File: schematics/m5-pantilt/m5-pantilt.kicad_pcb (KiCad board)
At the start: 2 copper layers, 50 x 50 mm, 28 parts, among them J1 Conn_02x15_Odd_Even, J2 Conn_02x03_Odd_Even, J3 Conn_02x03_Odd_Even, J4 Conn_01x04, J5 BAT, J6 Conn_01x04, J7 5V_POWER, SW1 SW_SPDT, U1 NL27WZ125

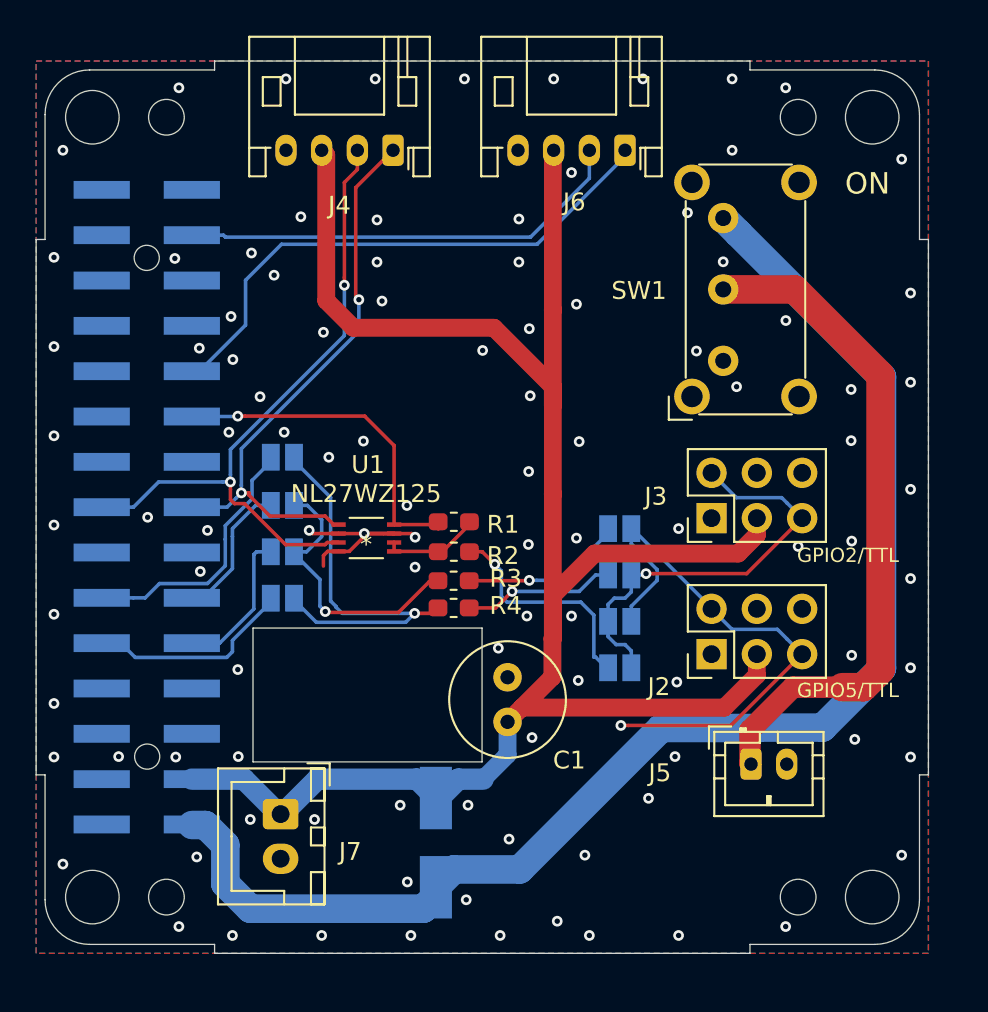
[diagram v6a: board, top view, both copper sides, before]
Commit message: Update to v0.2.0
Support another Three-State Bus Buffers, TC7WH241FK
Add description to schematic and PCB
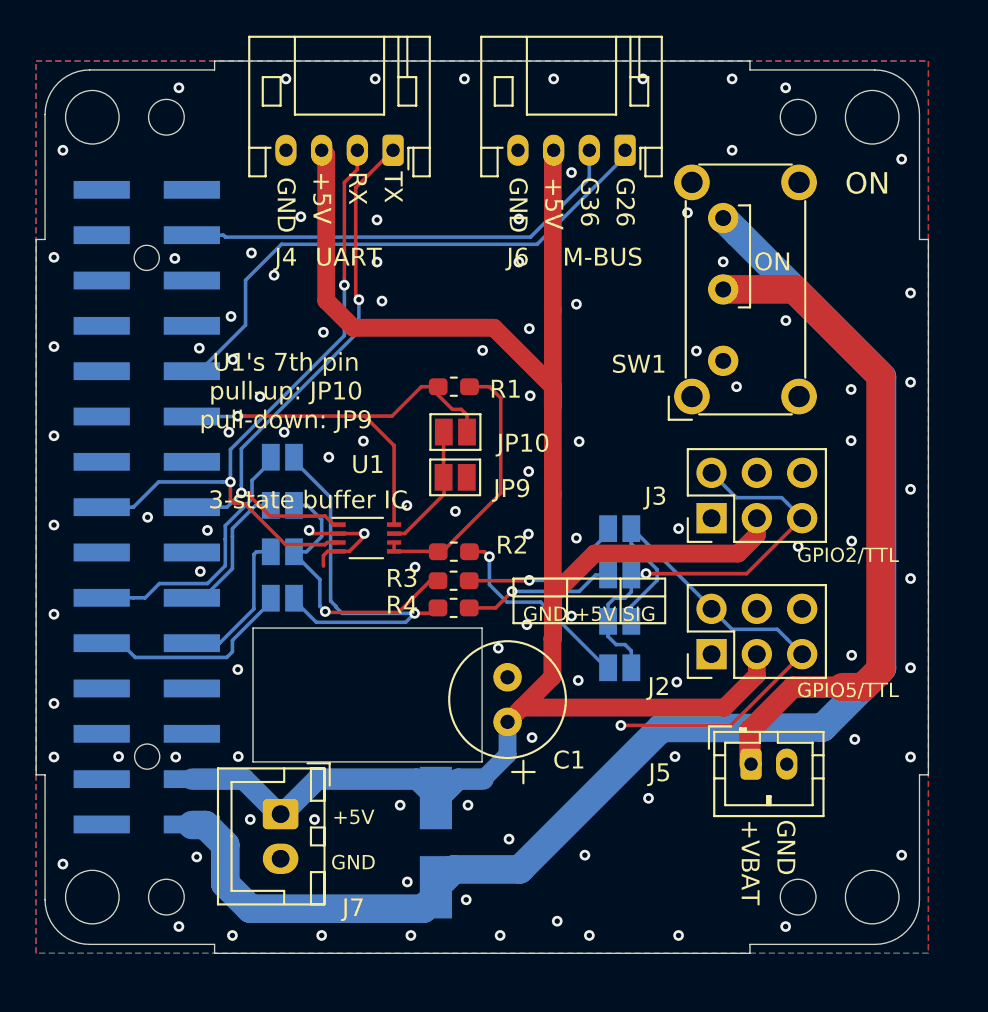
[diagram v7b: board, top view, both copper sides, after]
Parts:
- added JP10: Jumper_2_Open, Jumper:SolderJumper-2_P1.3mm_Open_Pad1.0x1.5mm, F.Cu at (123.5, 70.8)
- added JP9: Jumper_2_Open, Jumper:SolderJumper-2_P1.3mm_Open_Pad1.0x1.5mm, F.Cu at (123.5, 73.3)
- U1: value NL27WZ125 -> TC7WH241FK
- moved R1 7.57 mm to (123.4, 68.2)
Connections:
- U1 pad 7: GND -> Net-(JP10-Pad2)
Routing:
- net Net-(R1-Pad2): track 5.20 -> 15.4 mm
- net Net-(JP10-Pad2): track 0.00 -> 7.92 mm
- net +3V3: track 19.0 -> 25.1 mm
- net GND: track 11.2 -> 6.71 mm
- net Net-(JP4-Pad2): track 12.7 -> 11.4 mm
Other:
- board text added: "+5V"
- board text added: "+VBAT"
- board text added: "3-state buffer IC"
- board text added: "G26"
- board text added: "G36"
- board text added: "GND"
- board text added: "GND +5V SIG"
- board text added: "M-BUS"
- board text added: "RX"
- board text added: "TX"
- board text added: "U1's 7th pin pull-up: JP10 pull-down: JP9"
- board text added: "UART"
- board text added: "m5-pantilt board v0.2.0 @meganetaaan"
- board text removed: "m5-pantilt board v0.1.1 @meganetaaan"

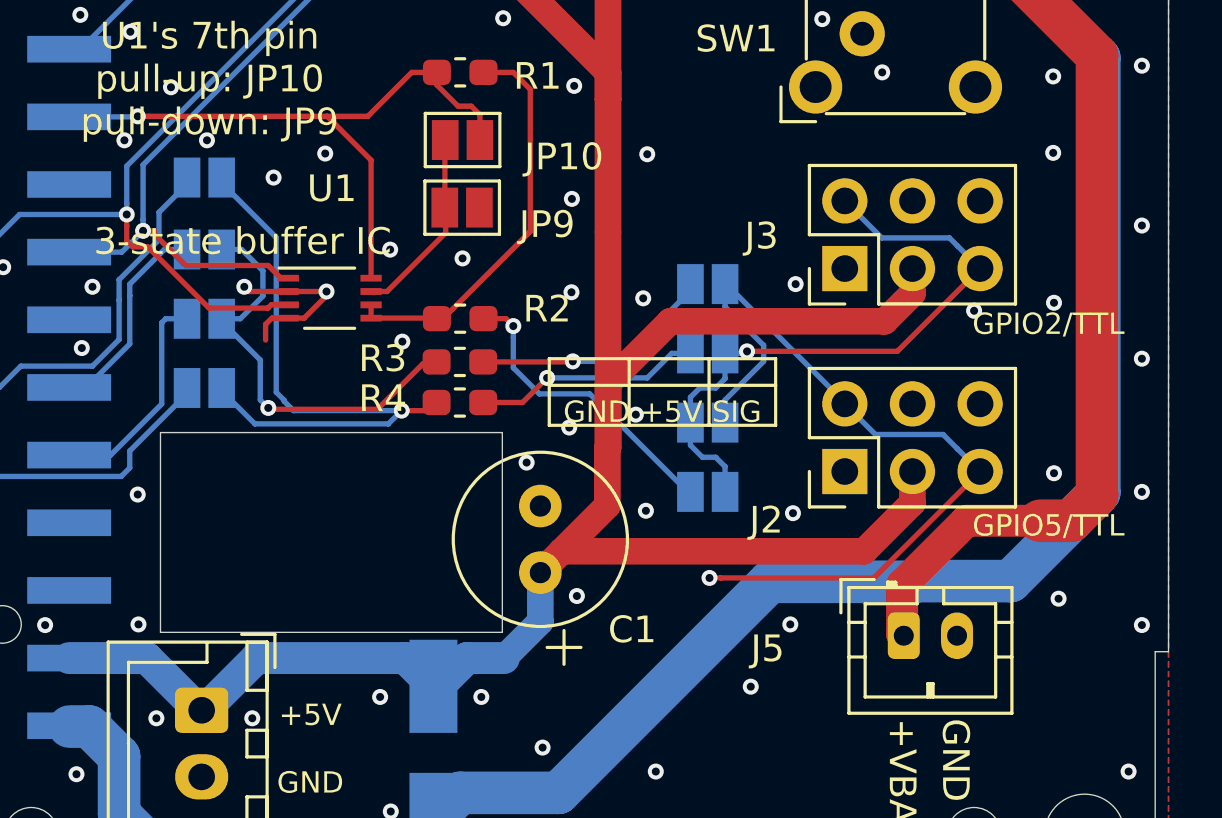
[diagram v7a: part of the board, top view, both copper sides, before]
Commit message: Use SMD MLCC for each servo power
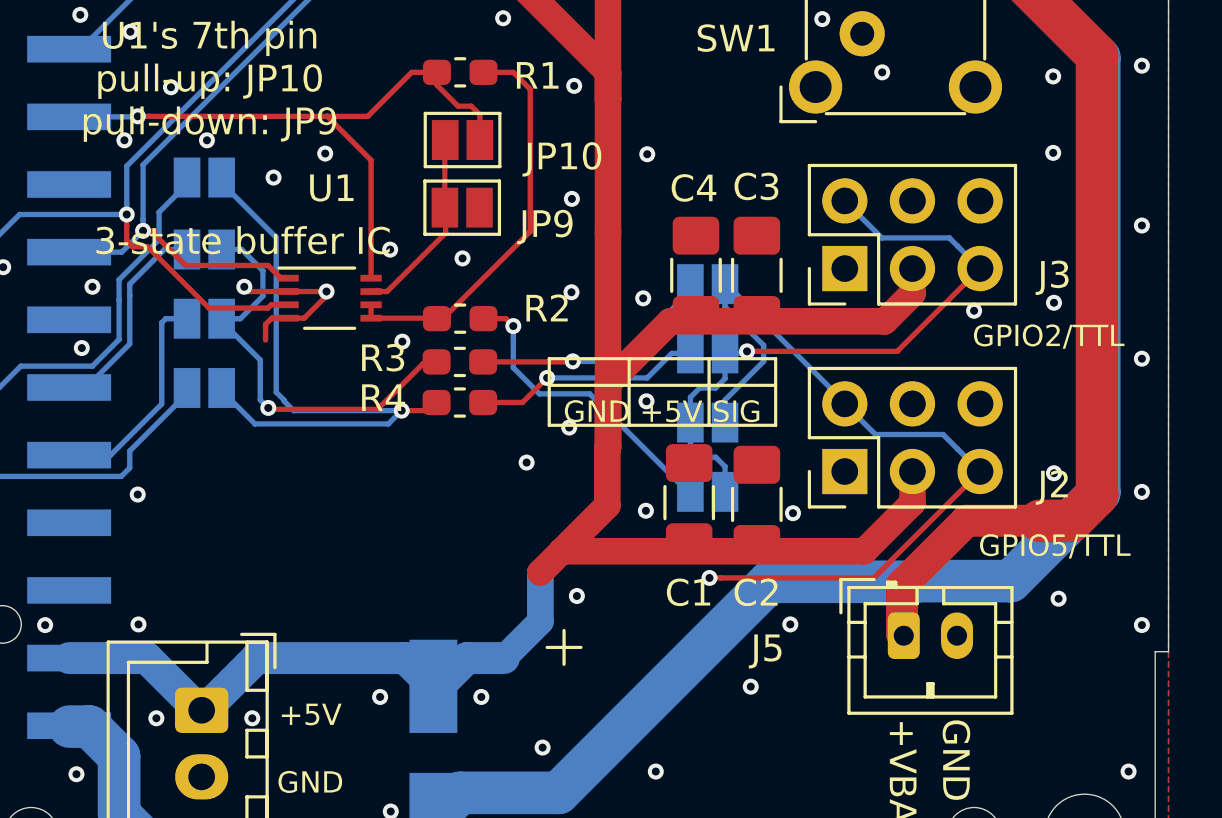
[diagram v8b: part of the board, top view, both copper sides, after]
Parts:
- removed LOGO: LOGO, m5-pantilt:avatar_small
- added C2: 100u, Capacitor_SMD:C_1206_3216Metric_Pad1.42x1.75mm_HandSolder, F.Cu at (134.5, 84.5)
- added C3: 100u, Capacitor_SMD:C_1206_3216Metric_Pad1.42x1.75mm_HandSolder, F.Cu at (134.5, 75.9)
- added C4: 100u, Capacitor_SMD:C_1206_3216Metric_Pad1.42x1.75mm_HandSolder, F.Cu at (132.3, 75.9)
- C1: footprint Capacitor_THT:C_Radial_D6.3mm_H11.0mm_P2.50mm -> Capacitor_SMD:C_1206_3216Metric_Pad1.42x1.75mm_HandSolder
- moved C1 5.59 mm to (132.0, 84.4)
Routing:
- net GND: vias 103 -> 102
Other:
- outline, holes or cut-outs redrawn
